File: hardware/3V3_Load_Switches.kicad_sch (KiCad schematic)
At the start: 28 parts, among them Q18 SI2302DDS-T1-GE3, Q19 SI2302DDS-T1-GE3, Q20 SI2302DDS-T1-GE3, U1 LMV321RIYLT, U2 INA199C1DCKR, U3 INA199C1DCKR, U4 INA199C1DCKR, U5 NVTFS5116PLTAG, U6 NVTFS5116PLTAG, U7 NVTFS5116PLTAG

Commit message: commit
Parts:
- removed R4: 33m, symbol Device:R_US
- removed R6, R7, R8: 30k, symbol Device:R_US
- added R221 (x3): 30k, footprints:CRCW060330K0FKEAHP, symbol CRCW060330K0FKEAHP:RES
- added R4: 33m, footprints:WSL2512R0330FEA18, symbol WSL2512R0330FEA18:RES
- R12, R13, R14: footprint (none) -> footprints:CRCW0603100KFKEAHP; symbol Device:R_US -> CRCW0603100KFKEAHP:CRCW0603100KFKEAHP; Arrow Part Number (none) -> CRCW0603100KFKEAHP; Arrow Price/Stock (none) -> https://www.arrow.com/en/products/crcw0603100kfkeahp/vishay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; Height (none) -> 0.55; Manufacturer_Name (none) -> Vishay; Manufacturer_Part_Number (none) -> CRCW0603100KFKEAHP; Mouser Part Number (none) -> 71-CRCW0603100KFKEAH; Mouser Price/Stock (none) -> https://www.mouser.co.uk/ProductDetail/Vishay-Dale/CRCW0603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
- R3: footprint (none) -> footprints:WSL2512R0330FEA18; symbol Device:R_US -> WSL2512R0330FEA18:RES
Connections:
- net +3V3: now also R3.1, R4.1; no longer R3.2
- net GND: now also R12.1, R13.1, R14.1; no longer R12.2, R13.2, R14.2
- net at U3.5 (IN-), U6.1, U6.2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: now also R221.2, R4.2
- net at Q20.3 (D), U6.4: now also R221.1
- net at R5.1, U4.5 (IN-), U7.1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: now also R221.2
- net at U2.5 (IN-), U5.1, U5.2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: now also R3.2, R221.2; no longer R3.1
- net at Q18.1 (G), R11.2: now also R14.2; no longer R14.1
- net at Q18.3 (D), U7.4: now also R221.1
- net at Q20.1 (G), R10.2: now also R13.2; no longer R13.1
- net at Q19.3 (D), U5.4: now also R221.1
- net at Q19.1 (G), R9.2: now also R12.2; no longer R12.1
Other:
- moved on the sheet: R12, R13, R14, R3

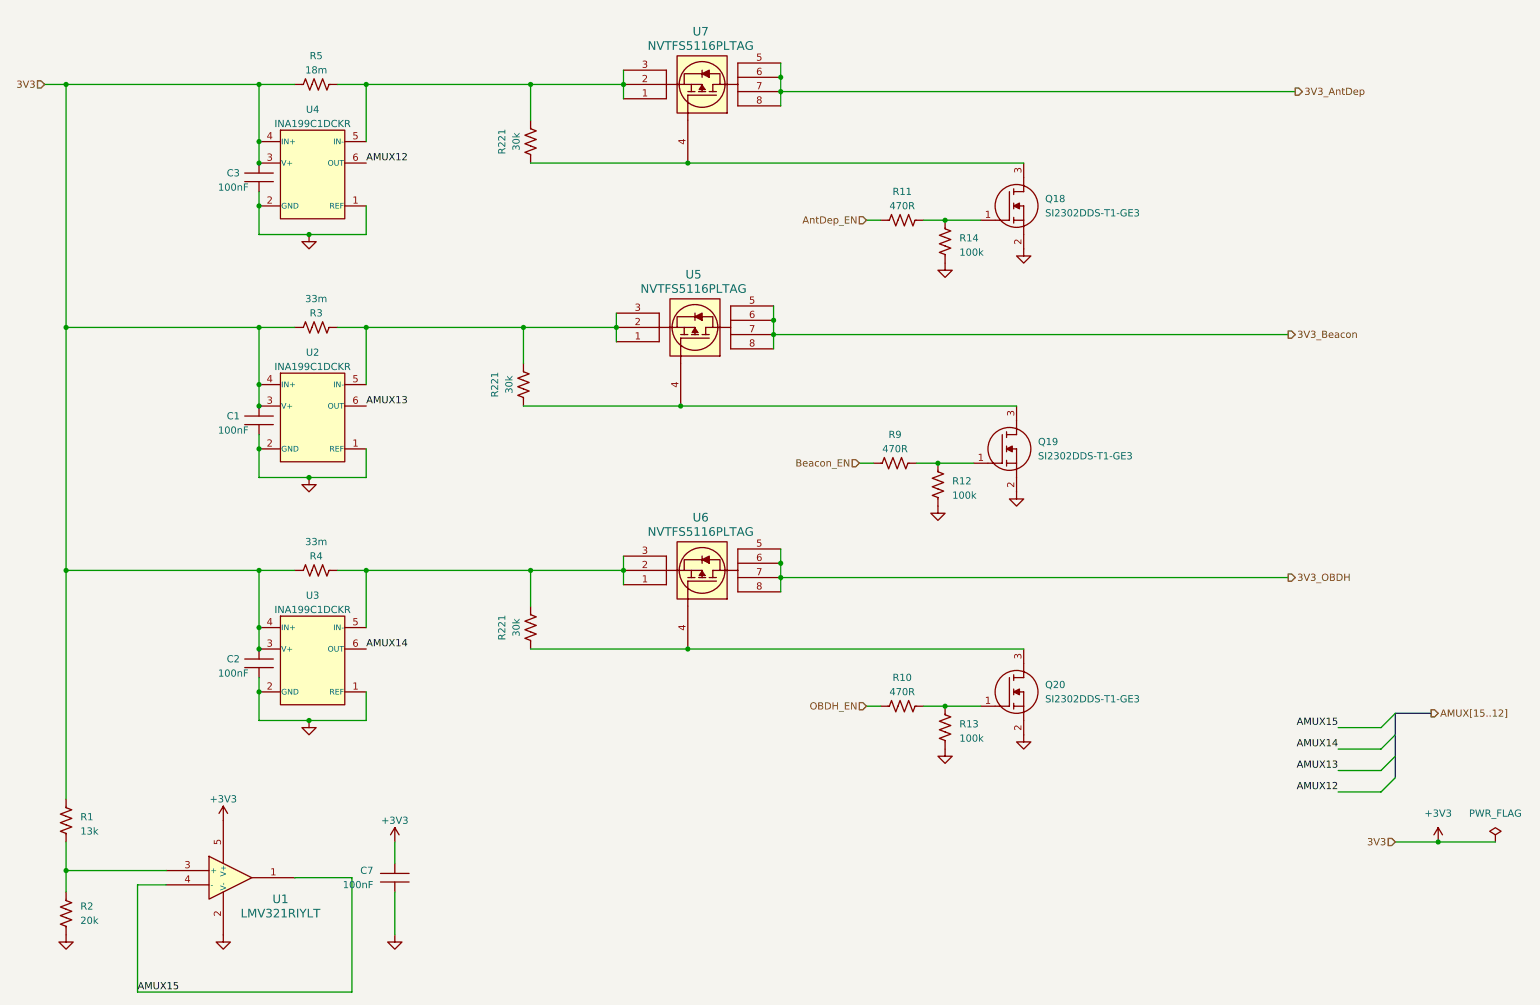
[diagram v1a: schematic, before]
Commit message: hardware: update in footprints
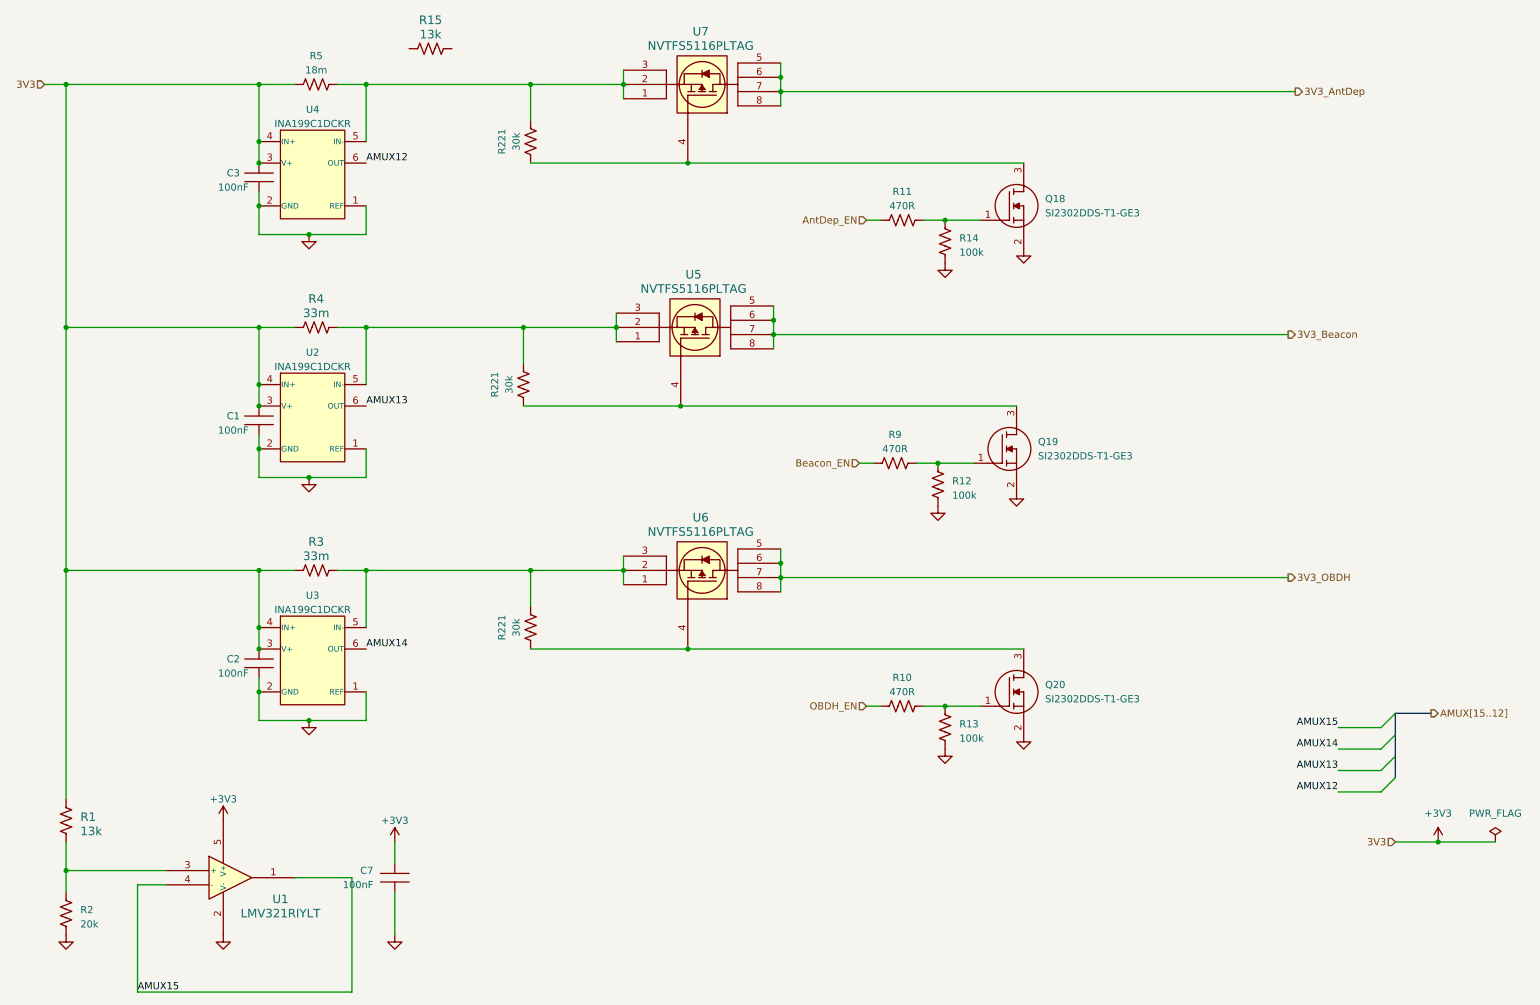
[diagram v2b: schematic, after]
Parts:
- removed R1: 13k, symbol Device:R_US
- removed R3, R4: 33m, footprints:WSL2512R0330FEA18, symbol WSL2512R0330FEA18:RES
- added R1, R15: 13k, footprints:CRCW060313K0FKEAHP, symbol CRCW060313K0FKEAHP:CRCW060313K0FKEAHP
- added R3, R4: 33m, footprints:WSL2010R0330FEA, symbol WSL2010R0330FEA:WSL2010R0330FEA
- R10, R11, R9: footprint (none) -> footprints:CRCW0603470RFKEAHP; symbol Device:R_US -> CRCW0603470RFKEAHP:CRCW0603470RFKEAHP; automotive (none) -> Yes; automotive grade (none) -> Grade 0; category (none) -> Res; composition (none) -> Thick Film; device class L1 (none) -> Passive Components; device class L2 (none) -> Resistors; device class L3 (none) -> Chip SMD Resistors; height (none) -> 0.55mm; ipc land pattern name (none) -> RESC16085X45; lead free (none) -> Yes; library id (none) -> 3843bba7e74bf2ed; manufacturer (none) -> Vishay; package (none) -> 0603; power (none) -> 250mW; power rating (none) -> 0.33W; resistance (none) -> 470Ω; rohs (none) -> Yes; series (none) -> CRCW-HP e3; temperature coefficient (none) -> 100ppm/°C; temperature range high (none) -> +155°C; temperature range low (none) -> -55°C; tolerance (none) -> 1%; voltage rating (none) -> 75V
- R2: footprint (none) -> footprints:CRCW060320K0FKEAHP; symbol Device:R_US -> CRCW060320K0FKEAHP:CRCW060320K0FKEAHP; automotive (none) -> Yes; automotive grade (none) -> Grade 0; category (none) -> Res; composition (none) -> Thick Film; device class L1 (none) -> Passive Components; device class L2 (none) -> Resistors; device class L3 (none) -> Chip SMD Resistors; height (none) -> 0.55mm; ipc land pattern name (none) -> RESC16085X45; lead free (none) -> Yes; library id (none) -> 6d0e00b833a89e4b; manufacturer (none) -> Vishay; package (none) -> 0603; power (none) -> 250mW; power rating (none) -> 0.33W; resistance (none) -> 20kΩ; rohs (none) -> Yes; series (none) -> CRCW-HP e3; temperature coefficient (none) -> 100ppm/°C; temperature range high (none) -> +155°C; temperature range low (none) -> -55°C; tolerance (none) -> 1%; voltage rating (none) -> 75V
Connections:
- net +3V3: now also R1.2, R3.1, R4.1
- net AntDep_EN: now also R11.2; no longer R11.1
- net Beacon_EN: now also R9.2; no longer R9.1
- net GND: now also R2.2; no longer R2.1
- net OBDH_EN: now also R10.2; no longer R10.1
- net at R221.2, U3.5 (IN-), U6.1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: now also R3.2
- net at R221.2, U2.5 (IN-), U5.1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: now also R4.2
- net at U1.3 (+): now also R2.1, R1.1; no longer R2.2
- net at Q18.1 (G), R14.2: now also R11.1; no longer R11.2
- net at Q20.1 (G), R13.2: now also R10.1; no longer R10.2
- net at Q19.1 (G), R12.2: now also R9.1; no longer R9.2
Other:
- moved on the sheet: R10, R11, R2, R9

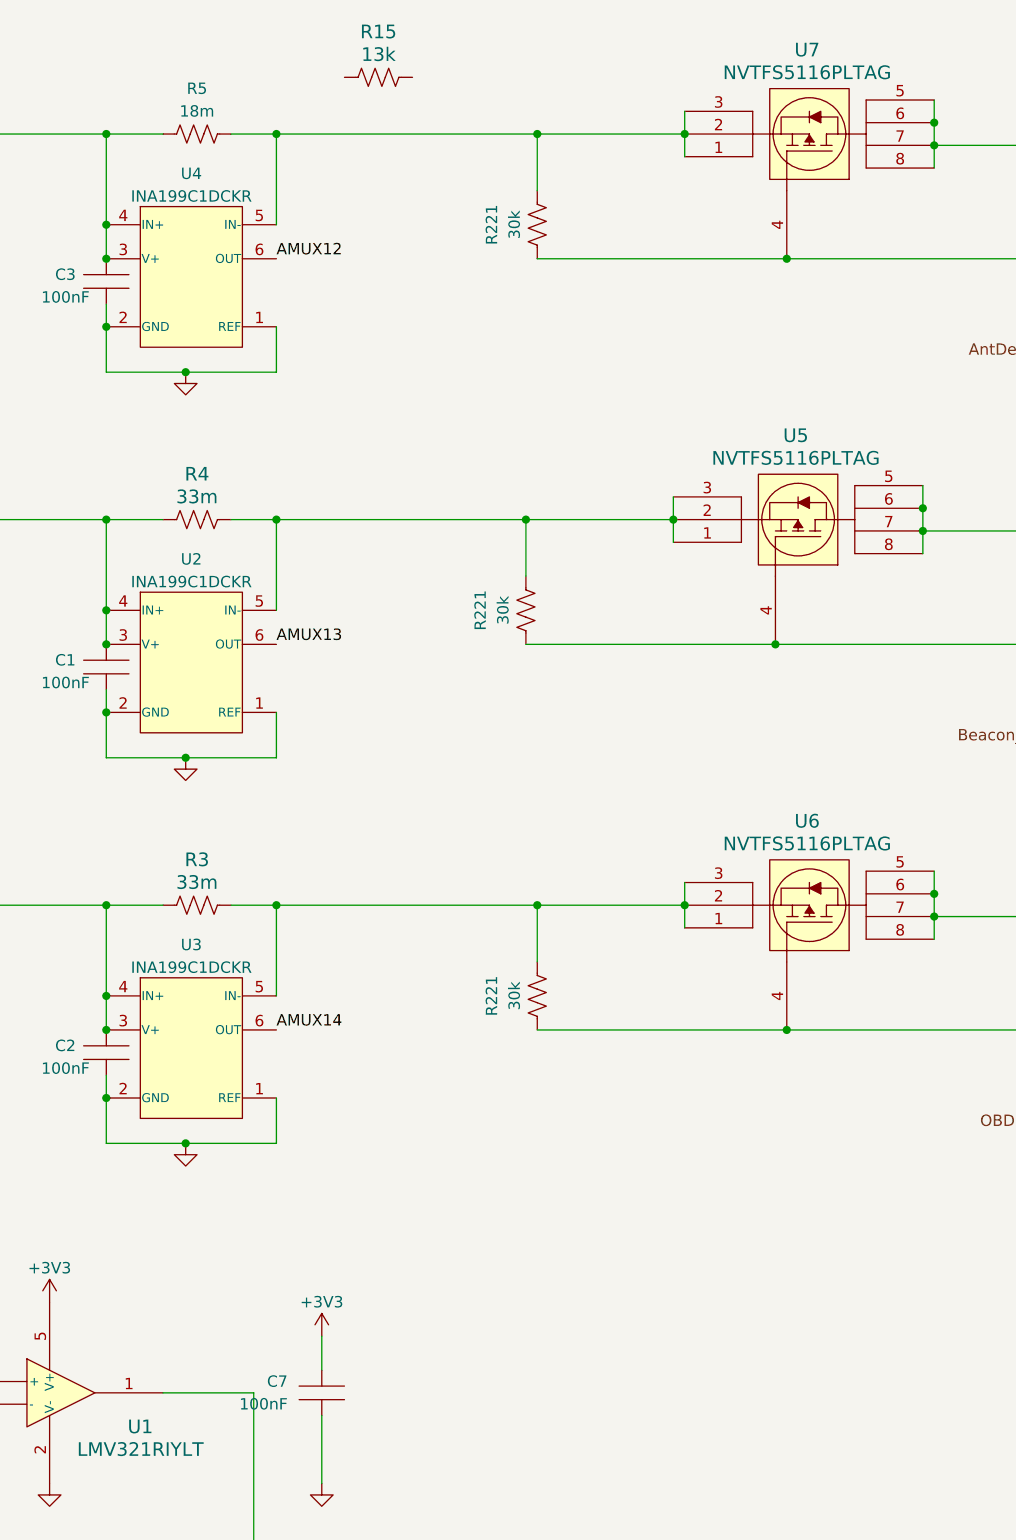
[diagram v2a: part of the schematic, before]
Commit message: hardware: All resistors added.
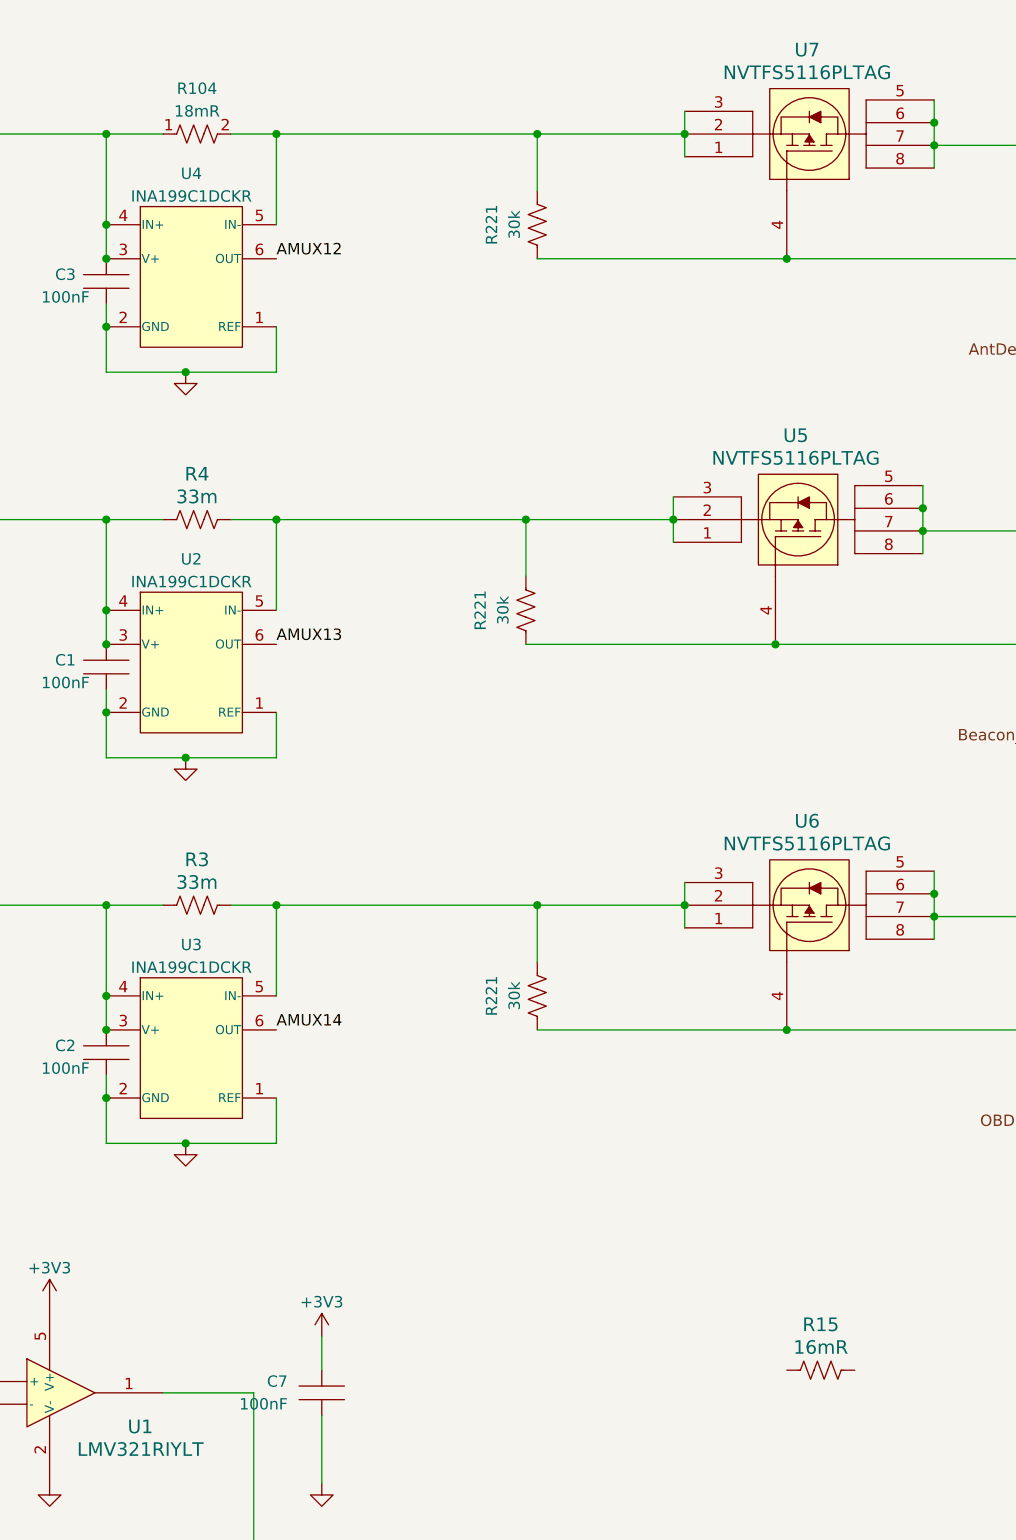
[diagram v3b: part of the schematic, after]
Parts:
- removed R15: 13k, footprints:CRCW060313K0FKEAHP, symbol CRCW060313K0FKEAHP:CRCW060313K0FKEAHP
- removed R5: 18m, symbol Device:R_US
- added R104: 18mR, RESC5125X89N, symbol WSL2010R0180FEA:WSL2010R0180FEA
- added R15: 16mR, footprints:WSL2010R0330FEA, symbol WSL2010R0160FEA:WSL2010R0160FEA
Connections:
- net +3V3: now also R104.1
- net at R221.2, U4.5 (IN-), U7.1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: now also R104.2
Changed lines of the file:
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@@
+    )
+  )
+  (symbol (lib_id "WSL2010R0180FEA:WSL2010R0180FEA") (at 58.42 27.94 0) (unit 1)
+    (in_bom yes) (on_board yes) (dnp no) (fields_autoplaced)
+    (property "Reference" "R104" (at 67.31 24.13 0)
+      (effects (font (size 1.27 1.27)))
+    )
+    (property "Value" "18mR" (at 67.31 26.67 0)
+      (effects (font (size 1.27 1.27)))
+    )
+    (property "Footprint" "RESC5125X89N" (at 72.39 124.13 0)
+      (effects (font (size 1.27 1.27)) (justify left top) hide)
+    )
+    (property "Datasheet" "https://www.arrow.com/en/products/wsl2010r0180fea/vishay" (at 72.39 224.13 0)
+      (effects (font (size 1.27 1.27)) (justify left top) hide)
+    )
+    (property "Height" "0.889" (at 72.39 424.13 0)
+      (effects (font (size 1.27 1.27)) (justify left top) hide)
+    )
+    (property "Mouser Part Number" "71-WSL2010R0180FEA" (at 72.39 524.13 0)
+      (effects (font (size 1.27 1.27)) (justify left top) hide)
+    )
+    (property "Mouser Price/Stock" "https://www.mouser.co.uk/ProductDetail/Vishay-Dale/WSL2010R0180FEA?qs=fncU5wK7Cm%2FkEWsMhCYm%252Bw%3D%3D" (at 72.39 624.13 0)
+      (effects (font (size 1.27 1.27)) (justify left top) hide)
+    )
+    (property "Manufacturer_Name" "Vishay" (at 72.39 724.13 0)
+      (effects (font (size 1.27 1.27)) (justify left top) hide)
+    )
+    (property "Manufacturer_Part_Number" "WSL2010R0180FEA" (at 72.39 824.13 0)
+      (effects (font (size 1.27 1.27)) (justify left top) hide)
+    )
+    (pin "1")
+    (pin "2")
+    (instances
+      (project "eps-re_project"
+        (path "/2eebaa11-d7ed-4bfd-bc8e-988f68654d29/091c188d-8c4a-409e-952c-8d45a0b217b0"
+          (reference "R104") (unit 1)
+        )
+        (path "/2eebaa11-d7ed-4bfd-bc8e-988f68654d29/b2d6a676-b7d9-423e-8a54-05279452700b"
+          (reference "R5") (unit 1)
+        )
+      )
     )
   )
@@
         (path "/9af6272d-3cb8-4e37-b792-5888e300588f"
           (reference "#PWR04") (unit 1)
-        )
-      )
-    )
-  )
-  (symbol (lib_id "Device:R_US") (at 67.31 29.21 270) (unit 1)
-    (in_bom yes) (on_board yes) (dnp no)
-    (property "Reference" "R5" (at 67.31 24.13 90)
-      (effects (font (size 1.27 1.27)))
-    )
-    (property "Value" "18m" (at 67.31 26.67 90)
-      (effects (font (size 1.27 1.27)))
-    )
-    (property "Footprint" "" (at 67.056 30.226 90)
-      (effects (font (size 1.27 1.27)) hide)
-    )
-    (property "Datasheet" "~" (at 67.31 29.21 0)
-      (effects (font (size 1.27 1.27)) hide)
-    )
-    (pin "1")
-    (pin "2")
-    (instances
-      (project "eps-re_project"
-        (path "/2eebaa11-d7ed-4bfd-bc8e-988f68654d29/b2d6a676-b7d9-423e-8a54-05279452700b"
-          (reference "R5") (unit 1)
-        )
-      )
-      (project "EPS Analogico"
-        (path "/9af6272d-3cb8-4e37-b792-5888e300588f"
-          (reference "R1") (unit 1)
         )
       )
@@
     )
   )
+  (symbol (lib_id "WSL2010R0160FEA:WSL2010R0160FEA") (at 130.81 167.64 0) (unit 1)
+    (in_bom yes) (on_board yes) (dnp no) (fields_autoplaced)
+    (property "Reference" "R15" (at 137.16 162.56 0)
+      (effects (font (size 1.524 1.524)))
+    )
+    (property "Value" "16mR" (at 137.16 165.1 0)
+      (effects (font (size 1.524 1.524)))
+    )
+    (property "Footprint" "footprints:WSL2010R0330FEA" (at 134.62 177.8 0)
+      (effects (font (size 1.27 1.27) italic) hide)
+    )
+    (property "Datasheet" "WSL2010R0330FEA" (at 135.89 175.26 0)
+      (effects (font (size 1.27 1.27) italic) hide)
+    )
+    (pin "1")
+    (pin "2")
+    (instances
+      (project "eps-re_project"
+        (path "/2eebaa11-d7ed-4bfd-bc8e-988f68654d29/b2d6a676-b7d9-423e-8a54-05279452700b"
+          (reference "R15") (unit 1)
+        )
+      )
+    )
+  )
   (symbol (lib_id "NVTFS5116PLWFTAG:NVTFS5116PLTAG") (at 148.59 92.71 270) (mirror x) (unit 1)
     (in_bom yes) (on_board yes) (dnp no)
@@
         )
       )
-    )
-  )
-  (symbol (lib_id "CRCW060313K0FKEAHP:CRCW060313K0FKEAHP") (at 81.28 22.86 0) (unit 1)
-    (in_bom yes) (on_board yes) (dnp no) (fields_autoplaced)
-    (property "Reference" "R15" (at 87.63 17.78 0)
-      (effects (font (size 1.524 1.524)))
-    )
-    (property "Value" "13k" (at 87.63 20.32 0)
-      (effects (font (size 1.524 1.524)))
-    )
-    (property "Footprint" "footprints:CRCW060313K0FKEAHP" (at 86.36 34.29 0)
-      (effects (font (size 1.27 1.27) italic) hide)
-    )
-    (property "Datasheet" "CRCW060313K0FKEAHP" (at 86.36 31.75 0)
-      (effects (font (size 1.27 1.27) italic) hide)
-    )
-    (pin "1")
-    (pin "2")
-    (instances
-      (project "eps-re_project"
-        (path "/2eebaa11-d7ed-4bfd-bc8e-988f68654d29/b2d6a676-b7d9-423e-8a54-05279452700b"
-          (reference "R15") (unit 1)
-        )
-      )
